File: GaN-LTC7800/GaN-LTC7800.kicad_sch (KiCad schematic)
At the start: 0 parts

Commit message: Schematics for Si and GaN for LTC7800 controller
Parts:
- added BFET_VGS, TFET_VGS: TestPoint_2Pole, symbol Connector:TestPoint_2Pole
- added C1: 0.05uF, symbol Device:C
- added C2, C6, CinA-1, CinA-2: 2.2uF, symbol Device:C
- added C3, C4: 0.1uF, symbol Device:C
- added C5: 10pF, symbol Device:C
- added C7: 100pF, symbol Device:C
- added CinB: 56uF, symbol Device:C_US
- added Cout: 100uF, symbol Device:C
- added D1: 1N47xxA, Diode_THT:D_DO-41_SOD81_P10.16mm_Horizontal, symbol Diode:1N47xxA
- added L1: 0.3uH, XGL1010-333MED:IND_XGL1010-333MED, symbol XGL1010-333MED:XGL1010-333MED
- added Q1, Q2: EPC2066, EPC_FETs:D0650, symbol EPC_FETs:EPC2066
- added R1: 100kOhm, symbol Device:R
- added R2: 25.5kOhm, symbol Device:R
- added R3: 3mOhm, symbol Device:R
- added R4: 100Ohm, symbol Device:R
- added R5: 50kOhm, symbol Device:R
- added R6: 312.5kOhm, symbol Device:R
- added R7: 5Ohm, symbol Device:R
- added R8: 3.92kOhm, symbol Device:R
- added TP_VIN, TP_VOUT: TestPoint, symbol Connector:TestPoint
- added U1: LTC7800HUDC_PBF, LTC7800HUDC_PBF:QFN50P400X300X80-21N, symbol LTC7800HUDC_PBF:LTC7800HUDC_PBF
- added VSource_GND, VSource_IN: 575-4, 5754, symbol 575-4:575-4
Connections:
- new net: C7.2, R8.2, U1.8 (ITH)
- new net: L1.2, R3.1, R4.1
- new net: C6.2, R8.1
- new net: C1.2, U1.19 (TRACK/SS)
- new net: R2.2, U1.20 (FREQ)
- new net: R1.1, U1.9 (PGOOD)
- new net BG: BFET_VGS.1, Q2.1 (G), U1.13 (BG)
- new net BOOST: C3.1, D1.1 (K), U1.12 (BOOST)
- new net GND: BFET_VGS.2, C1.1, C2.1, C6.1, C7.1, CinA-1.2, CinA-2.2, CinB.2, Cout.2, Q2.10 (S5), Q2.13 (S6), Q2.14 (S7), Q2.17 (S8), Q2.18 (S9), Q2.2 (S1), Q2.21 (S10), Q2.22 (S11), Q2.25 (S12), Q2.26 (S13), Q2.29 (S14), Q2.30 (Sub), Q2.5 (S2), Q2.6 (S3), Q2.9 (S4), R2.1, R5.2, R7.2, U1.15 (EXTVCC), U1.16 (PGND), U1.2 (SGND), U1.21 (SGND), U1.3 (SGND), VSource_GND.1
- new net INTVCC: C2.2, D1.2 (A), R1.2, U1.14 (INTVCC)
- new net SENSE+: C4.1, R4.2, U1.6 (SENSE+)
- new net SENSE-: C4.2, C5.1, Cout.1, R3.2, R6.1, R7.1, TP_VOUT.1, U1.5 (SENSE-)
- new net SW: C3.2, L1.1, Q1.10 (S5), Q1.13 (S6), Q1.14 (S7), Q1.17 (S8), Q1.18 (S9), Q1.2 (S1), Q1.21 (S10), Q1.22 (S11), Q1.25 (S12), Q1.26 (S13), Q1.29 (S14), Q1.30 (Sub), Q1.5 (S2), Q1.6 (S3), Q1.9 (S4), Q2.11 (D5), Q2.12 (D6), Q2.15 (D7), Q2.16 (D8), Q2.19 (D9), Q2.20 (D10), Q2.23 (D11), Q2.24 (D12), Q2.27 (D13), Q2.28 (D14), Q2.3 (D1), Q2.4 (D2), Q2.7 (D3), Q2.8 (D4), TFET_VGS.2, U1.11 (SW)
- new net TG: Q1.1 (G), TFET_VGS.1, U1.10 (TG)
- new net VFB: C5.2, R5.1, R6.2, U1.7 (VFB)
- new net VIN: CinA-1.1, CinA-2.1, CinB.1, Q1.11 (D5), Q1.12 (D6), Q1.15 (D7), Q1.16 (D8), Q1.19 (D9), Q1.20 (D10), Q1.23 (D11), Q1.24 (D12), Q1.27 (D13), Q1.28 (D14), Q1.3 (D1), Q1.4 (D2), Q1.7 (D3), Q1.8 (D4), TP_VIN.1, U1.17 (VIN), VSource_IN.1
- no-connect marks 0 -> 3

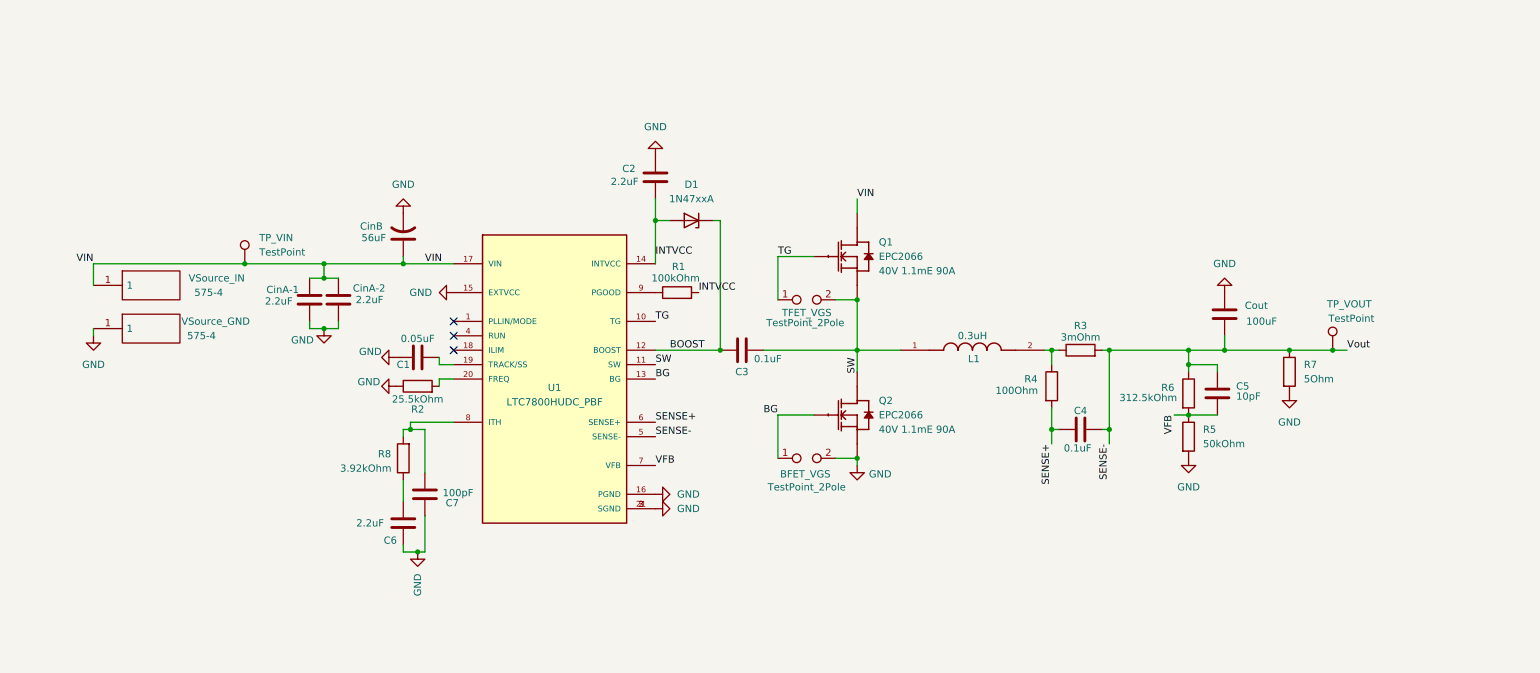
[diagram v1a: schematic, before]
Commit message: Updated footprints for LTC7800
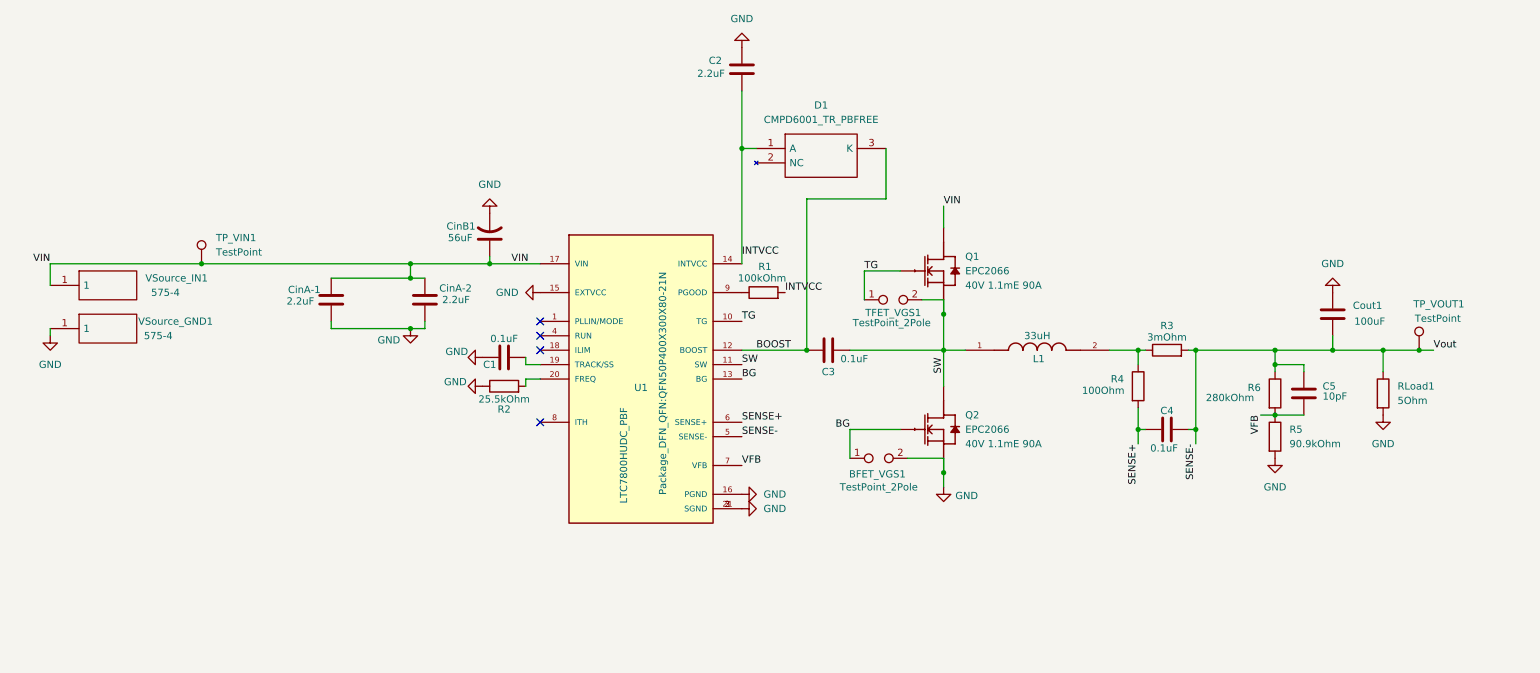
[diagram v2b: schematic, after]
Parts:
- removed C6: 2.2uF, symbol Device:C
- removed C7: 100pF, symbol Device:C
- removed D1: 1N47xxA, Diode_THT:D_DO-41_SOD81_P10.16mm_Horizontal, symbol Diode:1N47xxA
- removed R7: 5Ohm, symbol Device:R
- removed R8: 3.92kOhm, symbol Device:R
- added D1: CMPD6001_TR_PBFREE, Diode_SMD:SOT95P230X109-3N, symbol CMPD6001_TR_PBFREE:CMPD6001_TR_PBFREE
- added RLoad1: 5Ohm, Resistor_SMD:R_0201_0603Metric_Pad0.64x0.40mm_HandSolder, symbol Device:R
- BFET_VGS1: renamed from BFET_VGS; footprint (none) -> TestPoint:TestPoint_Bridge_Pitch2.54mm_Drill1.0mm
- C1: value 0.05uF -> 0.1uF; footprint (none) -> Capacitor_SMD:C_0805_2012Metric_Pad1.18x1.45mm_HandSolder
- C2, C3, C4, C5, CinA-1, CinA-2: footprint (none) -> Capacitor_SMD:C_0805_2012Metric_Pad1.18x1.45mm_HandSolder
- CinB1: renamed from CinB; footprint (none) -> Capacitor_SMD:C_0805_2012Metric_Pad1.18x1.45mm_HandSolder
- Cout1: renamed from Cout; footprint (none) -> Capacitor_SMD:C_0805_2012Metric_Pad1.18x1.45mm_HandSolder
- L1: value 0.3uH -> 33uH; footprint XGL1010-333MED:IND_XGL1010-333MED -> Inductor_SMD:IND_XGL1010-333MED
- Q1, Q2: footprint EPC_FETs:D0650 -> Transistor_Power:D0650
- R1, R2, R3, R4: footprint (none) -> Resistor_SMD:R_0201_0603Metric_Pad0.64x0.40mm_HandSolder
- R5: value 50kOhm -> 90.9kOhm; footprint (none) -> Resistor_SMD:R_0201_0603Metric_Pad0.64x0.40mm_HandSolder
- R6: value 312.5kOhm -> 280kOhm; footprint (none) -> Resistor_SMD:R_0201_0603Metric_Pad0.64x0.40mm_HandSolder
- TFET_VGS1: renamed from TFET_VGS; footprint (none) -> TestPoint:TestPoint_Bridge_Pitch2.54mm_Drill1.0mm
- TP_VIN1: renamed from TP_VIN; footprint (none) -> TestPoint:TestPoint_Loop_D2.60mm_Drill1.6mm_Beaded
- TP_VOUT1: renamed from TP_VOUT; footprint (none) -> TestPoint:TestPoint_Loop_D2.60mm_Drill1.6mm_Beaded
- U1: footprint LTC7800HUDC_PBF:QFN50P400X300X80-21N -> Package_DFN_QFN:QFN50P400X300X80-21N
- VSource_GND1: renamed from VSource_GND; footprint 5754 -> Battery:5754
- VSource_IN1: renamed from VSource_IN; footprint 5754 -> Battery:5754
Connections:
- net BOOST: now also D1.3 (K)
- net GND: now also RLoad1.2
- net INTVCC: now also D1.1 (A)
- net SENSE-: now also RLoad1.1
- no-connect marks 3 -> 4
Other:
- moved on the sheet: BFET_VGS1, C1, C2, C3, C4, C5, CinA-1, CinA-2, CinB1, Cout1, L1, Q1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

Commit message: Updated shematics
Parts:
- added C6: 100pF, Capacitor_SMD:C_0805_2012Metric_Pad1.18x1.45mm_HandSolder, symbol Device:C
- added CinA-E1, CinA-E10, CinA-E11, CinA-E12, CinA-E13, CinA-E14, CinA-E2, CinA-E3, CinA-E4, CinA-E5, CinA-E6, CinA-E7, CinA-E8, CinA-E9: ~, Capacitor_SMD:C_0805_2012Metric_Pad1.18x1.45mm_HandSolder, symbol Device:C
- added R7: 33kOhm, Resistor_SMD:R_0201_0603Metric_Pad0.64x0.40mm_HandSolder, symbol Device:R
- added R9: 3.92kOhm, Resistor_SMD:R_0201_0603Metric_Pad0.64x0.40mm_HandSolder, symbol Device:R
- C1: value 0.1uF -> 0.05uF
- C5: value 10pF -> 2.2uF
- R5: value 90.9kOhm -> 6.8kOhm
- R6: value 280kOhm -> 2.7kOhm
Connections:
- net BOOST: now also CinA-E8.2
- net GND: now also C5.1, C6.1, CinA-E1.2, CinA-E10.1, CinA-E11.1, CinA-E12.1, CinA-E13.1, CinA-E14.2, CinA-E2.2, CinA-E3.1, CinA-E4.1, CinA-E5.1, CinA-E6.2, CinA-E7.2
- net INTVCC: now also CinA-E7.1
- net SENSE+: now also CinA-E9.2
- net SENSE-: now also CinA-E11.2, CinA-E12.2, CinA-E9.1; no longer C5.1
- net SW: now also CinA-E8.1
- net VFB: now also R7.2; no longer C5.2, R6.2
- net VIN: now also CinA-E1.1, CinA-E14.1, CinA-E2.1, CinA-E4.2, CinA-E5.2, CinA-E6.1
- net at C1.2, U1.19 (TRACK/SS): now also CinA-E3.2
- net ITH: now reaches U1.8 (ITH)
- net ITH: now also C6.2, CinA-E13.2, R9.1
- new net: C5.2, CinA-E10.2, R9.2
- new net: R6.2, R7.1
- no-connect marks 4 -> 3
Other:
- moved on the sheet: BFET_VGS1, C1, C2, C3, C4, C5, CinA-1, CinA-2, CinB1, Cout1, D1, L1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

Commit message: Updated MOSFET
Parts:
- removed CinA-E1, CinA-E2, CinA-E4, CinA-E6: ~, Capacitor_SMD:C_0805_2012Metric_Pad1.18x1.45mm_HandSolder, symbol Device:C
- BFET_VGS1, TFET_VGS1: footprint TestPoint:TestPoint_Bridge_Pitch2.54mm_Drill1.0mm -> TestPoint:TestPoint_2Pads_Pitch2.54mm_Drill0.8mm
- renumbered CinA-1 to CinA1, CinA-2 to CinA2, CinA-E3 to E_C1, CinA-E7 to E_C2, CinA-E8 to E_C3, CinA-E9 to E_C4, CinA-E10 to E_C5, CinA-E13 to E_C6, CinA-E14 to Ex_Cin1, CinA-E5 to Ex_Cin2, CinA-E12 to Ex_Cout1, CinA-E11 to Ex_Cout2
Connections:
- net SENSE- renamed Vout
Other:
- moved on the sheet: BFET_VGS1, C1, C2, C3, C4, C5, C6, CinA1, CinA2, CinB1, Cout1, D1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

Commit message: Changed test points to header pins
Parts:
- removed TP_VIN1, TP_VOUT1: TestPoint, TestPoint:TestPoint_Loop_D2.60mm_Drill1.6mm_Beaded, symbol Connector:TestPoint
- added TP_VIN1, TP_VIN2, TP_VOUT1, TP_VOUT2: ~, Connector_PinHeader_2.54mm:PinHeader_1x01_P2.54mm_Vertical, symbol Connector:Conn_01x01_Pin
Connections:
- net GND: now also TP_VIN2.1 (Pin_1), TP_VOUT2.1 (Pin_1)
- net VIN: now also TP_VIN1.1 (Pin_1)
- net Vout: now also TP_VOUT1.1 (Pin_1)

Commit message: Changed font size and names on PCB
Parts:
- removed BFET_VGS1, TFET_VGS1: TestPoint_2Pole, TestPoint:TestPoint_2Pads_Pitch2.54mm_Drill0.8mm, symbol Connector:TestPoint_2Pole
- renumbered E_C1 to C1_EX1, E_C2 to C2_EX1, E_C3 to C3_EX1, E_C5 to C5_EX1, E_C6 to C6_EX1, Cout1 to COUT1, Ex_Cout1 to COUT_EX1, Ex_Cout2 to COUT_EX2, C4 to CSENSE1, E_C4 to CSENSE_EX1, Ex_Cin2 to CinA1_EX1, Ex_Cin1 to CinB1_EX1, TP_VOUT2 to GND1, RLoad1 to RLOAD1, R3 to RSENSE1, TP_VOUT1 to VOUT1
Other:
- moved on the sheet: CinB1_EX1, GND1, TP_VIN2
